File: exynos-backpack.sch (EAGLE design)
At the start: 21 parts, among them IC1 MIC5335-SPYMT, IC3 TXS0108ERGY

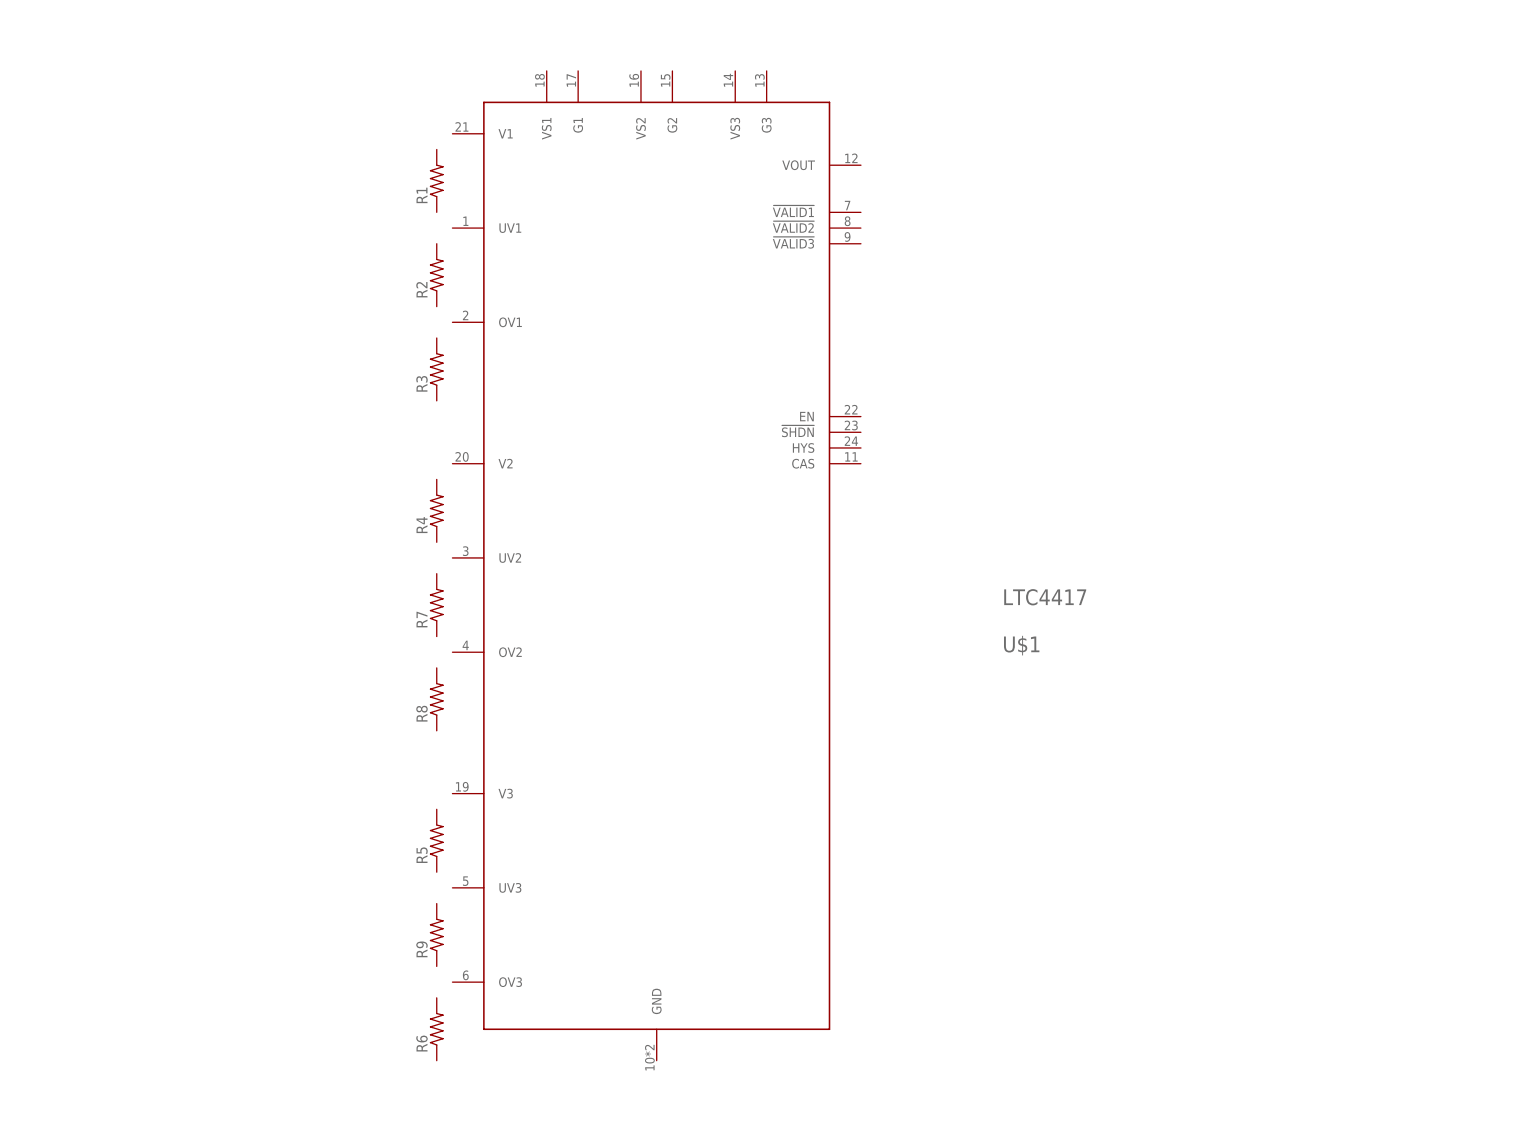
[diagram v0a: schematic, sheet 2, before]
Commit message: Update MOSFETs to Si7234DP in SPICE
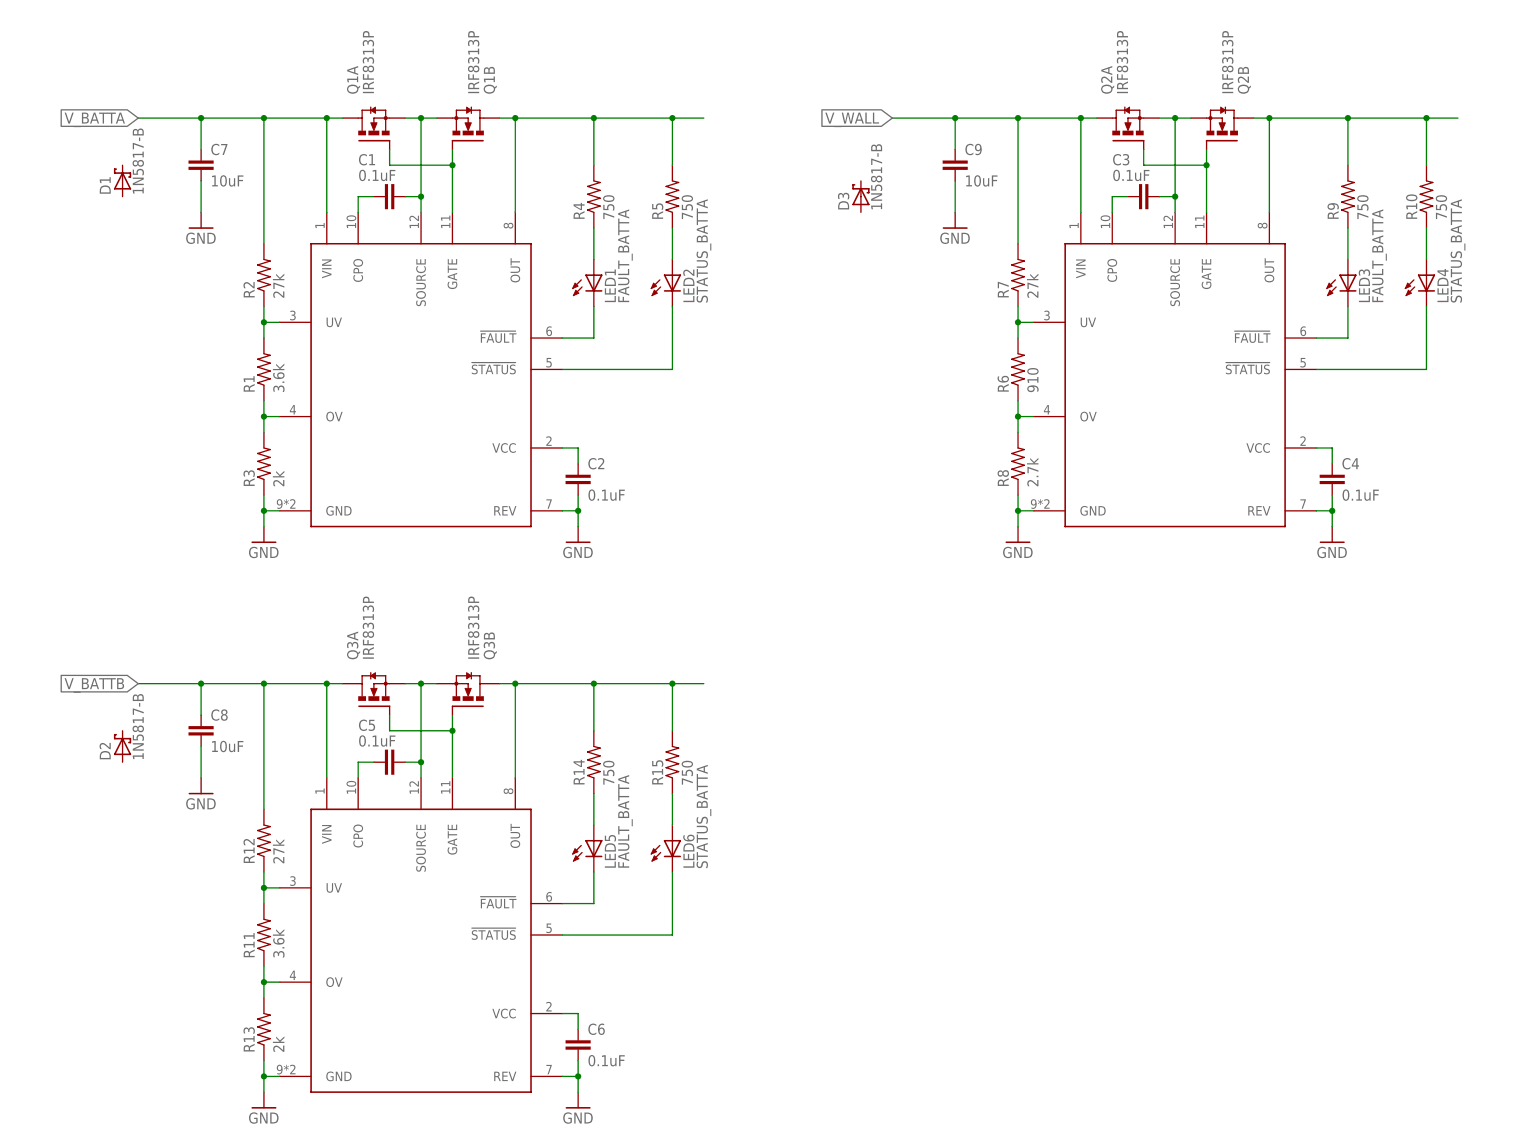
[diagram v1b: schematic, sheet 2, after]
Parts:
- added C1, C2, C3, C4, C5, C6: 0.1uF, biomimetic:CAP0402-CAP
- added C7, C8, C9: 10uF, biomimetic:CAP0402-CAP
- added D1, D2, D3: 1N5817-B, diode:1N5817-B
- added LED1, LED3, LED5: FAULT_BATTA, biomimetic:LED0603
- added LED2, LED4, LED6: STATUS_BATTA, biomimetic:LED0603
- added Q1, Q2, Q3: IRF8313P, transistor-power:IRF8313P
- added R10, R14, R15: 750, biomimetic:RESISTOR0402-RES
- added R11: 3.6k, biomimetic:RESISTOR0402-RES
- added R12: 27k, biomimetic:RESISTOR0402-RES
- added R13: 2k, biomimetic:RESISTOR0402-RES
- added U$2, U$3: LTC4352DD, biomimetic:LTC4352DD
- R1: value (none) -> 3.6k
- R2, R7: value (none) -> 27k
- R3: value (none) -> 2k
- R4, R5, R9: value (none) -> 750
- R6: value (none) -> 910
- R8: value (none) -> 2.7k
- U$1: value LTC4417 -> LTC4352DD; device biomimetic:LTC4417 -> biomimetic:LTC4352DD
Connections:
- new net N$1: C1.2, Q1A.S, Q1B.S, U$1.SOURCE
- new net N$10: LED2.C, U$1.!STATUS
- new net N$11: LED2.A, R5.1
- new net N$12: LED1.A, R4.1
- new net N$13: C3.2, Q2A.S, Q2B.S, U$2.SOURCE
- new net N$14: Q2A.G, Q2B.G, U$2.GATE
- new net N$15: C3.1, U$2.CPO
- new net N$17: Q2B.D, R10.2, R9.2, U$2.OUT
- new net N$18: R6.2, R7.1, U$2.UV
- new net N$19: R6.1, R8.2, U$2.OV
- new net N$2: Q1A.G, Q1B.G, U$1.GATE
- new net N$20: C4.1, U$2.VCC
- new net N$21: LED3.C, U$2.!FAULT
- new net N$22: LED4.C, U$2.!STATUS
- new net N$23: LED4.A, R10.1
- new net N$24: LED3.A, R9.1
- new net N$25: C5.2, Q3A.S, Q3B.S, U$3.SOURCE
- new net N$26: Q3A.G, Q3B.G, U$3.GATE
- new net N$27: C5.1, U$3.CPO
- new net N$29: Q3B.D, R14.2, R15.2, U$3.OUT
- new net N$30: R11.2, R12.1, U$3.UV
- new net N$31: R11.1, R13.2, U$3.OV
- new net N$32: C6.1, U$3.VCC
- new net N$33: LED5.C, U$3.!FAULT
- new net N$34: LED6.C, U$3.!STATUS
- new net N$35: LED6.A, R15.1
- new net N$36: LED5.A, R14.1
- new net N$4: C1.1, U$1.CPO
- new net N$5: Q1B.D, R4.2, R5.2, U$1.OUT
- new net N$6: R1.2, R2.1, U$1.UV
- new net N$7: R1.1, R3.2, U$1.OV
- new net N$8: C2.1, U$1.VCC
- new net N$9: LED1.C, U$1.!FAULT
- new net V_BATTA: C7.1, Q1A.D, R2.2, U$1.VIN
- new net V_BATTB: C8.1, Q3A.D, R12.2, U$3.VIN
- new net V_WALL: C9.1, Q2A.D, R7.2, U$2.VIN
- net GND: now also C2.2, C4.2, C6.2, C7.2, C8.2, C9.2, R13.1, R3.1, R8.1, U$1.GND, U$1.REV, U$2.GND, U$2.REV, U$3.GND, U$3.REV
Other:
- moved on the sheet: R1, R2, R3, R4, R5, R6, R7, R8, R9

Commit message: Add ODROID-U2 drawing
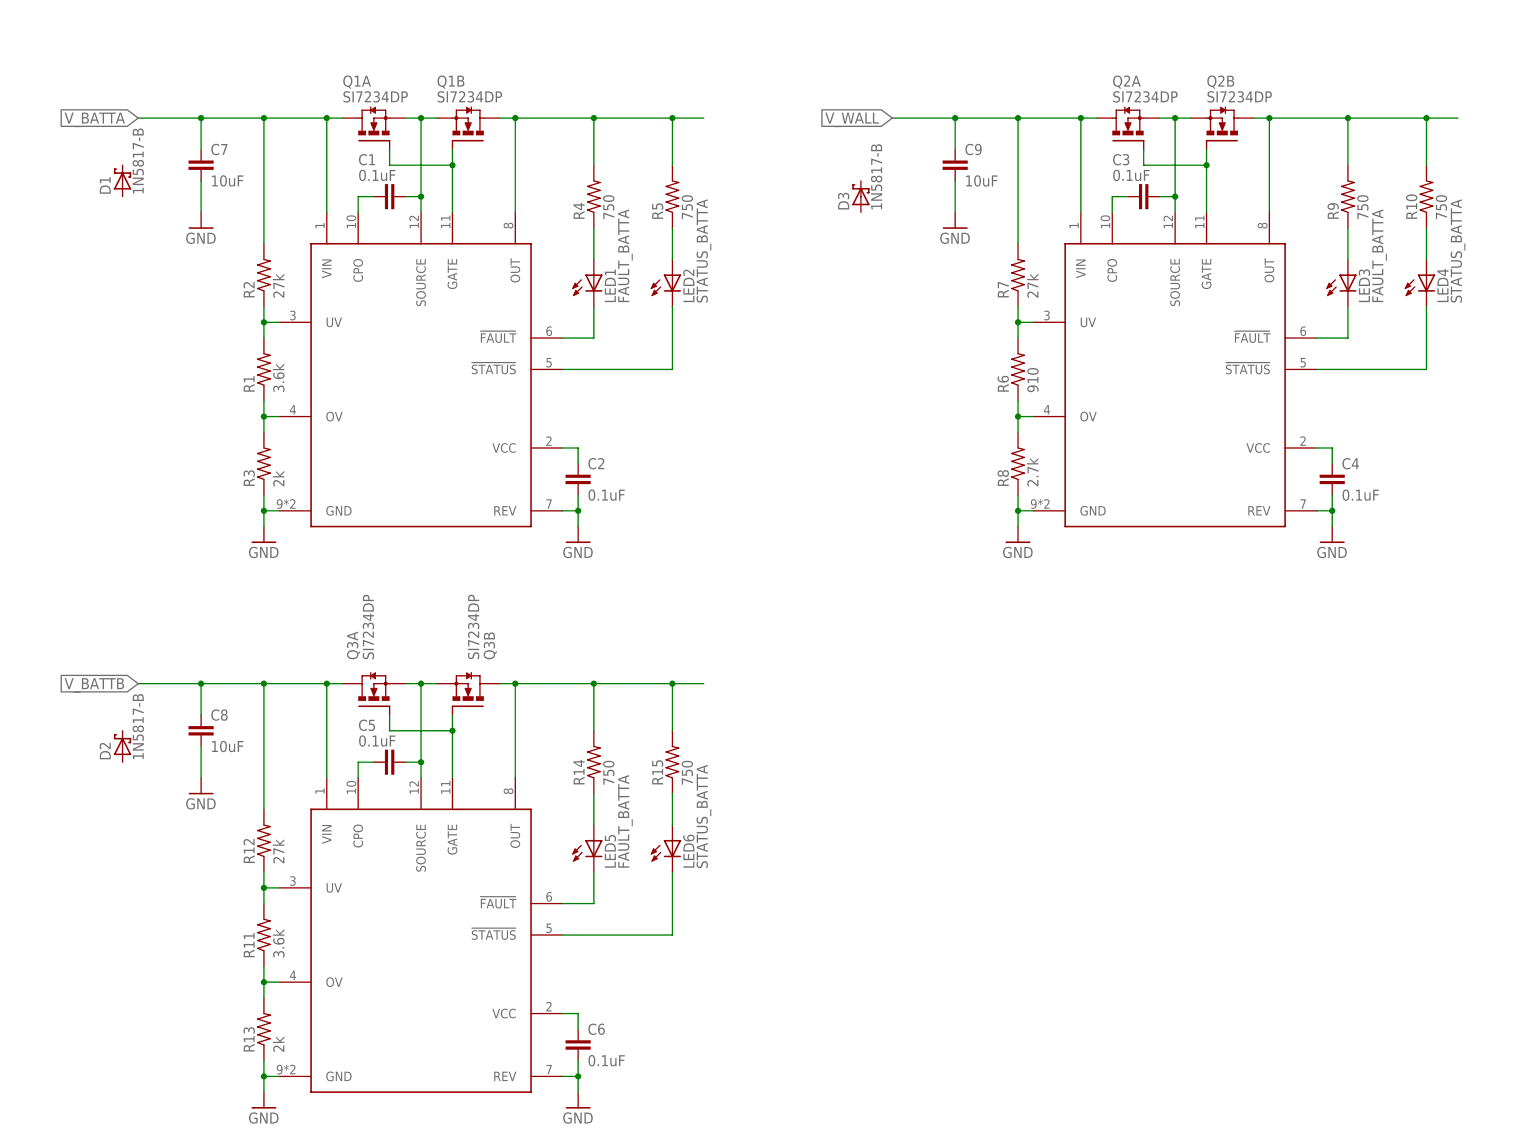
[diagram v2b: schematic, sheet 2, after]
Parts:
- Q1, Q2, Q3: value IRF8313P -> SI7234DP; device transistor-power:IRF8313P -> biomimetic:SI7234DP
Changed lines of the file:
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@@
 <part name="R2" library="biomimetic" deviceset="RESISTOR" device="0402-RES" value="27k"/>
 <part name="R3" library="biomimetic" deviceset="RESISTOR" device="0402-RES" value="2k"/>
-<part name="Q1" library="transistor-power" deviceset="IRF8313P" device=""/>
+<part name="Q1" library="biomimetic" deviceset="SI7234DP" device=""/>
 <part name="C1" library="biomimetic" deviceset="CAP" device="0402-CAP" value="0.1uF"/>
 <part name="C2" library="biomimetic" deviceset="CAP" device="0402-CAP" value="0.1uF"/>
@@
 <part name="R7" library="biomimetic" deviceset="RESISTOR" device="0402-RES" value="27k"/>
 <part name="R8" library="biomimetic" deviceset="RESISTOR" device="0402-RES" value="2.7k"/>
-<part name="Q2" library="transistor-power" deviceset="IRF8313P" device=""/>
+<part name="Q2" library="biomimetic" deviceset="SI7234DP" device=""/>
 <part name="C3" library="biomimetic" deviceset="CAP" device="0402-CAP" value="0.1uF"/>
 <part name="C4" library="biomimetic" deviceset="CAP" device="0402-CAP" value="0.1uF"/>
@@
 <part name="R12" library="biomimetic" deviceset="RESISTOR" device="0402-RES" value="27k"/>
 <part name="R13" library="biomimetic" deviceset="RESISTOR" device="0402-RES" value="2k"/>
-<part name="Q3" library="transistor-power" deviceset="IRF8313P" device=""/>
+<part name="Q3" library="biomimetic" deviceset="SI7234DP" device=""/>
 <part name="C5" library="biomimetic" deviceset="CAP" device="0402-CAP" value="0.1uF"/>
 <part name="C6" library="biomimetic" deviceset="CAP" device="0402-CAP" value="0.1uF"/>
@@
 <instance part="R2" gate="G$1" x="40.64" y="139.7" rot="R90"/>
 <instance part="R3" gate="G$1" x="40.64" y="109.22" rot="R90"/>
-<instance part="Q1" gate="A" x="58.42" y="162.56" rot="R90"/>
-<instance part="Q1" gate="B" x="73.66" y="162.56" rot="MR90"/>
+<instance part="Q1" gate="A" x="58.42" y="162.56" smashed="yes" rot="R90">
+<attribute name="NAME" x="53.34" y="170.18" size="1.778" layer="95"/>
+<attribute name="VALUE" x="53.34" y="167.64" size="1.778" layer="96"/>
+</instance>
+<instance part="Q1" gate="B" x="73.66" y="162.56" smashed="yes" rot="MR90">
+<attribute name="NAME" x="68.58" y="170.18" size="1.778" layer="95" rot="MR180" align="top-left"/>
+<attribute name="VALUE" x="68.58" y="167.64" size="1.778" layer="96" rot="MR180" align="top-left"/>
+</instance>
 <instance part="C1" gate="G$1" x="60.96" y="152.4" smashed="yes" rot="R90">
 <attribute name="NAME" x="55.88" y="157.48" size="1.778" layer="95"/>
@@
 <instance part="R7" gate="G$1" x="162.56" y="139.7" rot="R90"/>
 <instance part="R8" gate="G$1" x="162.56" y="109.22" rot="R90"/>
-<instance part="Q2" gate="A" x="180.34" y="162.56" rot="R90"/>
-<instance part="Q2" gate="B" x="195.58" y="162.56" rot="MR90"/>
+<instance part="Q2" gate="A" x="180.34" y="162.56" smashed="yes" rot="R90">
+<attribute name="NAME" x="177.8" y="170.18" size="1.778" layer="95"/>
+<attribute name="VALUE" x="177.8" y="167.64" size="1.778" layer="96"/>
+</instance>
+<instance part="Q2" gate="B" x="195.58" y="162.56" smashed="yes" rot="MR90">
+<attribute name="NAME" x="193.04" y="170.18" size="1.778" layer="95" rot="MR180" align="top-left"/>
+<attribute name="VALUE" x="193.04" y="167.64" size="1.778" layer="96" rot="MR180" align="top-left"/>
+</instance>
 <instance part="C3" gate="G$1" x="182.88" y="152.4" smashed="yes" rot="R90">
 <attribute name="NAME" x="177.8" y="157.48" size="1.778" layer="95"/>
@@
 <instance part="R12" gate="G$1" x="40.64" y="48.26" rot="R90"/>
 <instance part="R13" gate="G$1" x="40.64" y="17.78" rot="R90"/>
-<instance part="Q3" gate="A" x="58.42" y="71.12" rot="R90"/>
-<instance part="Q3" gate="B" x="73.66" y="71.12" rot="MR90"/>
+<instance part="Q3" gate="A" x="58.42" y="71.12" smashed="yes" rot="R90">
+<attribute name="NAME" x="55.88" y="77.47" size="1.778" layer="95" rot="R90"/>
+<attribute name="VALUE" x="58.42" y="77.47" size="1.778" layer="96" rot="R90"/>
+</instance>
+<instance part="Q3" gate="B" x="73.66" y="71.12" smashed="yes" rot="MR90">
+<attribute name="NAME" x="76.2" y="77.47" size="1.778" layer="95" rot="MR90"/>
+<attribute name="VALUE" x="73.66" y="77.47" size="1.778" layer="96" rot="MR90"/>
+</instance>
 <instance part="C5" gate="G$1" x="60.96" y="60.96" smashed="yes" rot="R90">
 <attribute name="NAME" x="55.88" y="66.04" size="1.778" layer="95"/>

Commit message: Add TVS protection diodes
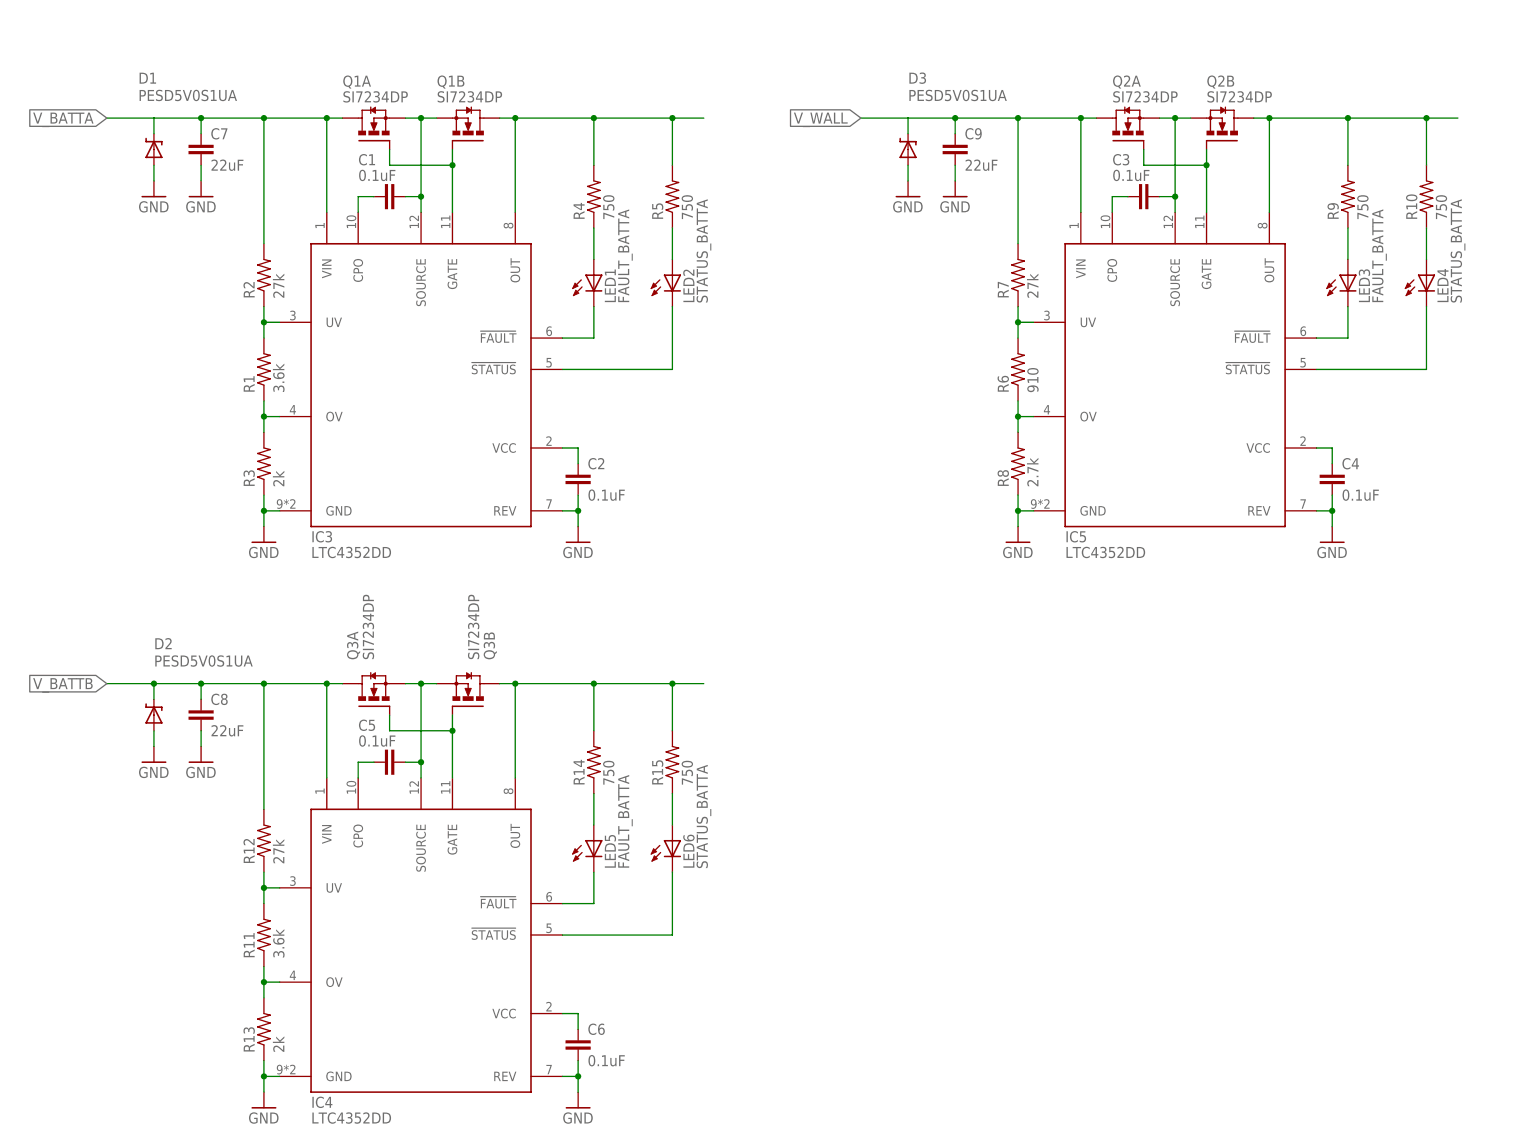
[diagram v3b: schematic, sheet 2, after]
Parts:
- removed U$1: LTC4352DD, biomimetic:LTC4352DD
- added IC2: TXS0108ERGY, biomimetic:TXS0108ERGY
- C7, C8, C9: value 10uF -> 22uF
- D1, D2, D3: value 1N5817-B -> PESD5V0S1UA; device diode:1N5817-B -> biomimetic:PESD5V0S1UA
- IC3: value TXS0108ERGY -> LTC4352DD; device biomimetic:TXS0108ERGY -> biomimetic:LTC4352DD
- renumbered U$2 to IC5, U$3 to IC4
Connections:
- net 1.8V: now also IC2.OE, IC2.VCCA; no longer IC3.OE, IC3.VCCA
- net 3.3V: now also IC2.VCCB; no longer IC3.VCCB
- net GND: now also D1.A, D2.A, D3.A, IC2.GND, IC3.REV; no longer U$1.GND, U$1.REV
- net N$1: now also IC3.SOURCE; no longer U$1.SOURCE
- net N$10: now also IC3.!STATUS; no longer U$1.!STATUS
- net N$2: now also IC3.GATE; no longer U$1.GATE
- net N$4: now also IC3.CPO; no longer U$1.CPO
- net N$5: now also IC3.OUT; no longer U$1.OUT
- net N$6: now also IC3.UV; no longer U$1.UV
- net N$7: now also IC3.OV; no longer U$1.OV
- net N$8: now also IC3.VCC; no longer U$1.VCC
- net N$9: now also IC3.!FAULT; no longer U$1.!FAULT
- net UART_RX_1V8: now also IC2.A2; no longer IC3.A2
- net UART_RX_3V3: now also IC2.B2; no longer IC3.B2
- net UART_TX_1V8: now also IC2.A1; no longer IC3.A1
- net UART_TX_3V3: now also IC2.B1; no longer IC3.B1
- net V_BATTA: now also D1.C, IC3.VIN; no longer U$1.VIN
- net V_BATTB: now also D2.C
- net V_WALL: now also D3.C
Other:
- moved on the sheet: C7, C8, C9
